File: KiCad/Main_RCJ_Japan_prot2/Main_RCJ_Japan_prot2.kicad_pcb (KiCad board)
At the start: 2 copper layers, 13 parts, among them J1 Conn_01x04_Socket, J2 Conn_01x04_Socket, J3 Conn_01x04_Socket, J4 Conn_01x04_Socket, J5 Conn_01x04_Socket, J6 Conn_01x04_Socket

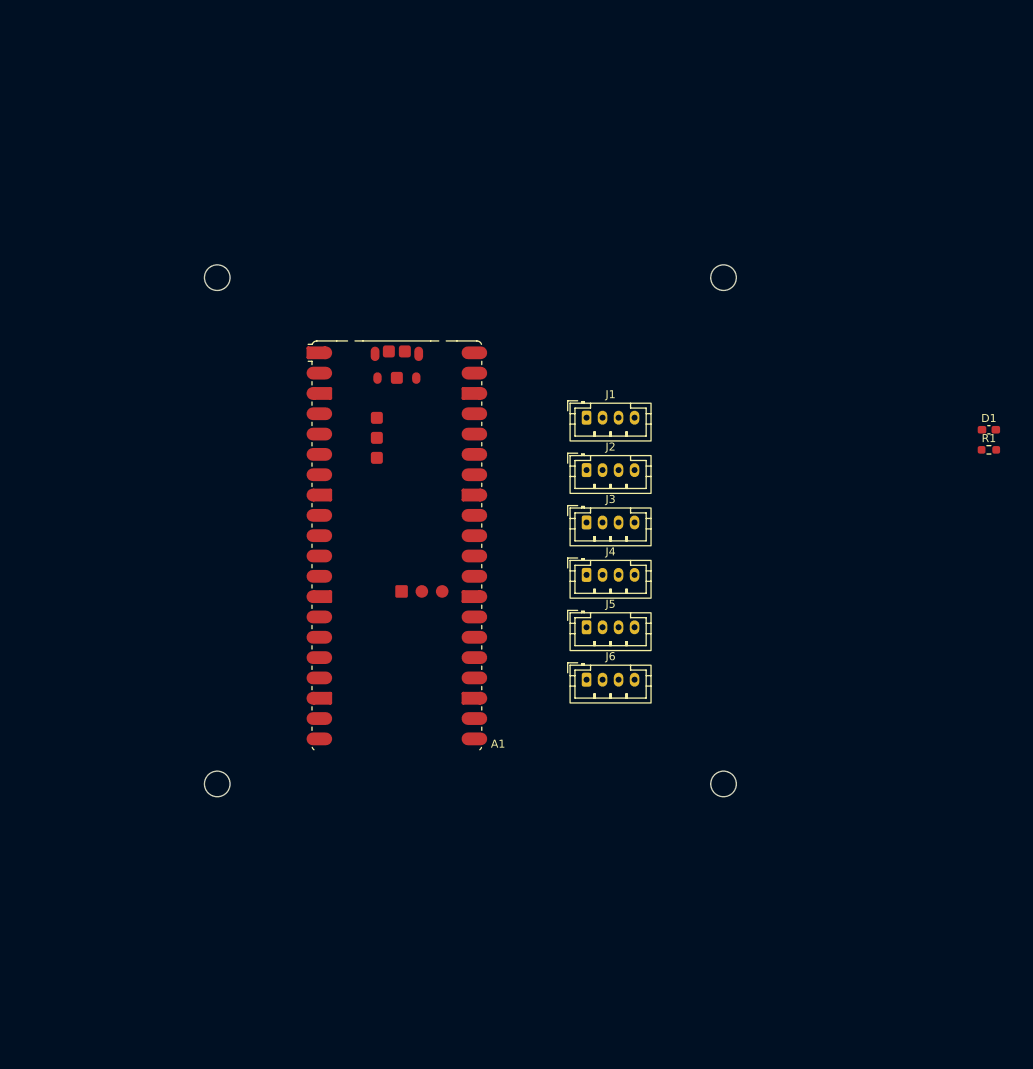
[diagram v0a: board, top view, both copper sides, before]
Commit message: 新メイン仮配置完了
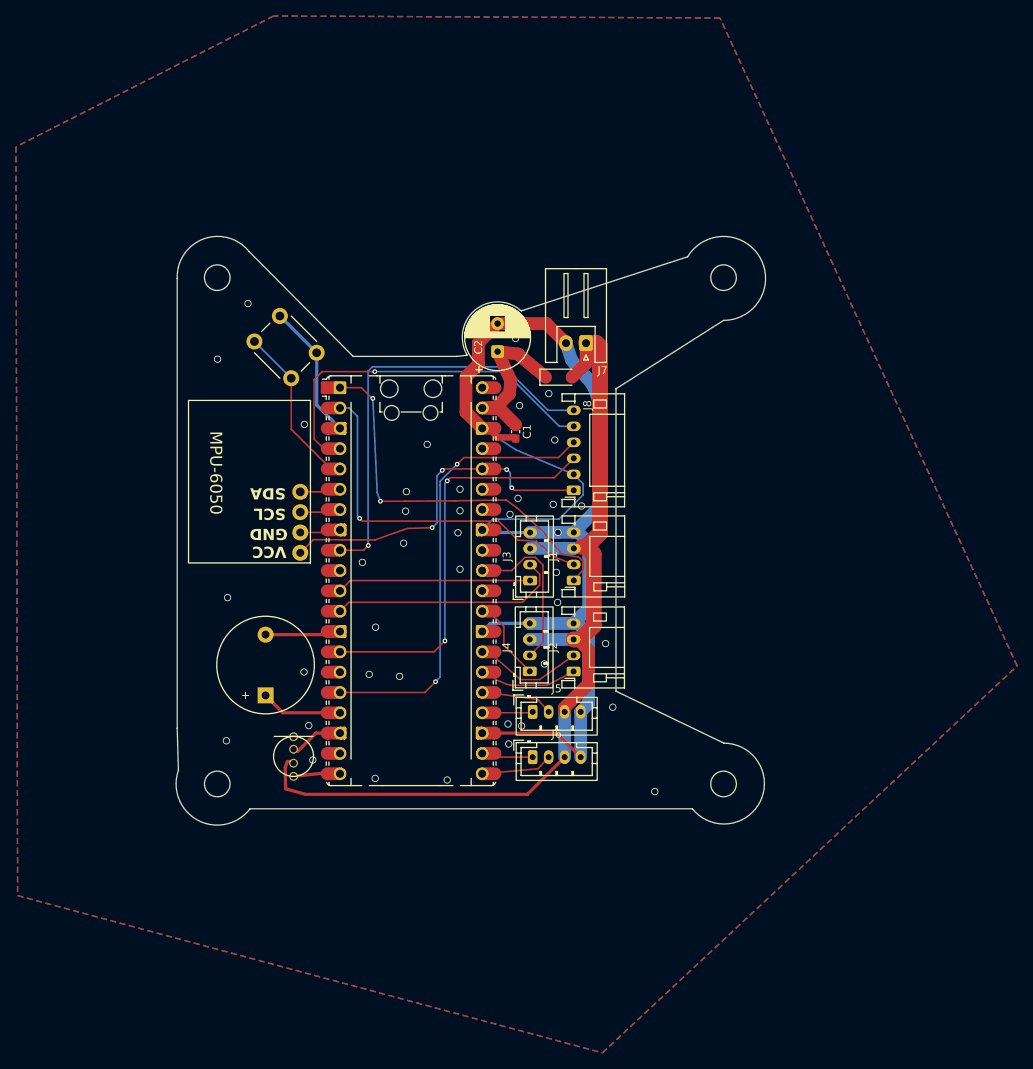
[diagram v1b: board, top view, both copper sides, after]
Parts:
- removed D1: LED, Capacitor_SMD:C_0603_1608Metric_Pad1.08x0.95mm_HandSolder
- removed R1: R, Resistor_SMD:R_0603_1608Metric_Pad0.98x0.95mm_HandSolder
- added BZ1: Buzzer, Buzzer_Beeper:Buzzer_12x9.5RM7.6, F.Cu at (74.4, 120.6)
- added C1: C, Capacitor_SMD:C_0603_1608Metric_Pad1.08x0.95mm_HandSolder, F.Cu at (105.7, 87.6)
- added C2: C_Polarized_US, Capacitor_THT:CP_Radial_D8.0mm_P3.50mm, F.Cu at (103.4, 77.6)
- added D2: D_Schottky, Diode_SMD:D_SOD-123, F.Cu at (111.0, 80.8)
- added J7: Conn_01x02_Socket, Connector_JST:JST_XH_S2B-XH-A_1x02_P2.50mm_Horizontal, F.Cu at (114.5, 76.5)
- added J8: Conn_01x06_Socket, Connector_JST:JST_PH_S6B-PH-K_1x06_P2.00mm_Horizontal, F.Cu at (112.9, 94.9)
- added SW1: SW_Push, Button_Switch_THT:SW_PUSH_6mm, F.Cu at (76.2, 73.2)
- added U1: ~, MPU:名称未設定, F.Cu at (73.7, 97.7)
- added U2: ~, PL9823-F5(RGBLED):名称未設定, F.Cu at (77.9, 128.2)
- A1: footprint Module:RaspberryPi_Pico_W_SMD -> Module:RaspberryPi_Pico_Common_Unspecified
- J1, J2: footprint Connector_JST:JST_PH_B4B-PH-K_1x04_P2.00mm_Vertical -> Connector_JST:JST_PH_S4B-PH-K_1x04_P2.00mm_Horizontal
- moved J2 25.2 mm to (112.9, 117.6), turned to 90 degrees
- moved J1 20.4 mm to (112.9, 106.2), turned to 90 degrees
- moved J4 14.0 mm to (107.4, 117.6), turned to 90 degrees
- moved J5 12.5 mm to (107.8, 122.6)
- moved J6 11.8 mm to (107.8, 128.3)
- moved J3 10.1 mm to (107.5, 106.2), turned to 90 degrees
- moved A1 4.71 mm to (92.6, 106.2)
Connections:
- A1 pad 14: unconnected-(A1-GPIO10-Pad14) -> kicker_in1
- A1 pad 16: unconnected-(A1-GPIO12-Pad16) -> kicker_in2
- A1 pad 17: unconnected-(A1-GPIO13-Pad17) -> Net-(A1-GPIO13)
- A1 pad 20: unconnected-(A1-GPIO15-Pad20) -> Net-(A1-GPIO15)
- A1 pad 21: unconnected-(A1-GPIO16-Pad21) -> PIO-UART3_RX
- A1 pad 22: unconnected-(A1-GPIO17-Pad22) -> PIO-UART3_TX
- A1 pad 24: unconnected-(A1-GPIO18-Pad24) -> PIO-UART2_TX
- A1 pad 25: unconnected-(A1-GPIO19-Pad25) -> PIO-UART2_RX
- A1 pad 26: unconnected-(A1-GPIO20-Pad26) -> PIO-UART0_TX
- A1 pad 27: unconnected-(A1-GPIO21-Pad27) -> PIO-UART0_RX
- A1 pad 29: unconnected-(A1-GPIO22-Pad29) -> PIO-UART1_TX
- A1 pad 31: unconnected-(A1-GPIO26_ADC0-Pad31) -> PIO-UART1_RX
- A1 pad 36: unconnected-(A1-3V3-Pad36) -> 3v3
- A1 pad 39: VCC -> Net-(A1-VSYS)
- A1 pad 4: unconnected-(A1-GPIO2-Pad4) -> kicker_in3
- A1 pad 5: unconnected-(A1-GPIO3-Pad5) -> Net-(A1-GPIO3)
- A1 pad 9: unconnected-(A1-GPIO6-Pad9) -> kicker_in4
- J1 pad 1: unconnected-(J1-Pin_1-Pad1) -> UART0_TX
- J1 pad 2: unconnected-(J1-Pin_2-Pad2) -> UART0_RX
- J1 pad 3: unconnected-(J1-Pin_3-Pad3) -> VCC
- J1 pad 4: unconnected-(J1-Pin_4-Pad4) -> GND
- J2 pad 1: unconnected-(J2-Pin_1-Pad1) -> PIO-UART0_TX
- J2 pad 2: unconnected-(J2-Pin_2-Pad2) -> PIO-UART0_RX
- J2 pad 3: unconnected-(J2-Pin_3-Pad3) -> VCC
- J2 pad 4: unconnected-(J2-Pin_4-Pad4) -> GND
- J3 pad 1: unconnected-(J3-Pin_1-Pad1) -> H-UART1_TX
- J3 pad 2: unconnected-(J3-Pin_2-Pad2) -> H-UART1_RX
- J3 pad 3: unconnected-(J3-Pin_3-Pad3) -> VCC
- J3 pad 4: unconnected-(J3-Pin_4-Pad4) -> GND
- J4 pad 1: unconnected-(J4-Pin_1-Pad1) -> PIO-UART1_TX
- J4 pad 2: unconnected-(J4-Pin_2-Pad2) -> PIO-UART1_RX
- J4 pad 3: unconnected-(J4-Pin_3-Pad3) -> VCC
- J4 pad 4: unconnected-(J4-Pin_4-Pad4) -> GND
- J5 pad 1: unconnected-(J5-Pin_1-Pad1) -> PIO-UART2_TX
- J5 pad 2: unconnected-(J5-Pin_2-Pad2) -> PIO-UART2_RX
- J5 pad 3: unconnected-(J5-Pin_3-Pad3) -> VCC
- J5 pad 4: unconnected-(J5-Pin_4-Pad4) -> GND
- J6 pad 1: unconnected-(J6-Pin_1-Pad1) -> PIO-UART3_TX
- J6 pad 2: unconnected-(J6-Pin_2-Pad2) -> PIO-UART3_RX
- J6 pad 3: unconnected-(J6-Pin_3-Pad3) -> VCC
- J6 pad 4: unconnected-(J6-Pin_4-Pad4) -> GND
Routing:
- net GND: track 0.00 -> 193.3 mm, vias 0 -> 40
- net VCC: track 0.00 -> 115.8 mm
- net kicker_in2: track 0.00 -> 57.1 mm, vias 0 -> 2
- net kicker_in4: track 0.00 -> 53.8 mm, vias 0 -> 1
- net kicker_in1: track 0.00 -> 50.8 mm, vias 0 -> 2
- net UART0_TX: track 0.00 -> 48.8 mm, vias 0 -> 2
- net kicker_in3: track 0.00 -> 46.1 mm, vias 0 -> 1
- net UART0_RX: track 0.00 -> 44.7 mm, vias 0 -> 1
- net 3v3: track 0.00 -> 43.7 mm, vias 0 -> 4
- net H-UART1_RX: track 0.00 -> 29.4 mm
- net H-UART1_TX: track 0.00 -> 24.3 mm
- net Net-(A1-VSYS): track 0.00 -> 21.1 mm
- net Net-(A1-GPIO3): track 0.00 -> 21.0 mm
- net PIO-UART1_RX: track 0.00 -> 20.6 mm
- net PIO-UART0_RX: track 0.00 -> 12.9 mm
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- added copper zone on B.Cu, net GND
- added copper zone on F.Cu, net GND
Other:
- board outline added: 73.7 x 73.6 mm

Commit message: 新メイン完成
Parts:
- added C3: C, Capacitor_SMD:C_0603_1608Metric_Pad1.08x0.95mm_HandSolder, F.Cu at (66.1, 109.6)
- added G***: LOGO, LOGO:名称未設定, F.Cu at (86.5, 137.8)
- added G***: LOGO, LOGO:ICON, F.Cu at (96.6, 144.1)
- added G***: LOGO, LOGO:logo, F.Cu at (111.7, 59.4)
- added J10: Conn_01x02_Socket, Connector_JST:JST_XH_S2B-XH-A_1x02_P2.50mm_Horizontal, F.Cu at (124.6, 137.7)
- added J11: Conn_01x03_Socket, Connector_JST:JST_PH_B3B-PH-K_1x03_P2.00mm_Vertical, F.Cu at (99.9, 127.2)
- added J12: Conn_01x03_Socket, Connector_JST:JST_PH_B3B-PH-K_1x03_P2.00mm_Vertical, F.Cu at (99.9, 115.6)
- added J13: Conn_01x02_Socket, Connector_JST:JST_PH_B2B-PH-K_1x02_P2.00mm_Vertical, F.Cu at (100.9, 121.4)
- added J14: Conn_01x02_Socket, Connector_JST:JST_PH_B2B-PH-K_1x02_P2.00mm_Vertical, F.Cu at (100.3, 133.2)
- added J9: Conn_02x03_Odd_Even, Connector_PinHeader_2.54mm:PinHeader_2x03_P2.54mm_Vertical, F.Cu at (60.3, 77.5)
- added R1: R, Resistor_THT:R_Axial_DIN0309_L9.0mm_D3.2mm_P12.70mm_Horizontal, F.Cu at (116.9, 139.2)
- added R2: R, Resistor_THT:R_Axial_DIN0309_L9.0mm_D3.2mm_P12.70mm_Horizontal, F.Cu at (118.3, 143.5)
- moved SW1 54.0 mm to (80.6, 127.0), turned to 0 degrees
- moved J8 24.1 mm to (98.0, 76.0)
- moved BZ1 18.0 mm to (59.3, 110.7), turned to -90 degrees
- moved C1 16.9 mm to (91.7, 78.1)
- moved J3 15.6 mm to (94.0, 98.4)
- moved A1 15.6 mm to (79.1, 98.5)
- moved J1 15.6 mm to (99.5, 98.4)
- moved J2 15.6 mm to (99.4, 109.8)
- moved J4 15.6 mm to (94.0, 109.8)
- moved J7 15.5 mm to (102.8, 86.8), turned to 90 degrees
- moved J6 14.3 mm to (94.0, 132.0), turned to 90 degrees
- moved J5 13.9 mm to (94.0, 120.9), turned to 90 degrees
- moved U1 13.0 mm to (61.1, 101.0)
- moved D2 11.0 mm to (100.1, 80.0)
- moved C2 10.0 mm to (95.4, 83.7), turned to -90 degrees
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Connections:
- A1 pad 10: unconnected-(A1-GPIO7-Pad10) -> Net-(A1-GPIO7)
- A1 pad 15: unconnected-(A1-GPIO11-Pad15) -> PIO-UART1_RX
- A1 pad 19: unconnected-(A1-GPIO14-Pad19) -> Net-(A1-GPIO14)
- A1 pad 31: PIO-UART1_RX -> ADC1
- A1 pad 32: unconnected-(A1-GPIO27_ADC1-Pad32) -> ADC2
- A1 pad 34: unconnected-(A1-GPIO28_ADC2-Pad34) -> BATT_ADC
- U2 pad 3: VCC -> Net-(A1-VSYS)
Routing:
- net 3v3: track 43.7 -> 148.9 mm, vias 4 -> 3
- net Net-(A1-VSYS): track 21.1 -> 126.0 mm, vias 0 -> 1
- net BATT_ADC: track 0.00 -> 68.5 mm, vias 0 -> 3
- net ADC1: track 0.00 -> 52.8 mm
- net GND: track 193.3 -> 245.9 mm, vias 40 -> 69
- net Net-(A1-GPIO14): track 0.00 -> 49.4 mm
- net ADC2: track 0.00 -> 48.6 mm
- net VCC: track 115.8 -> 72.3 mm
- net Net-(A1-GPIO3): track 21.0 -> 59.4 mm, vias 0 -> 1
- net Net-(A1-GPIO7): track 0.00 -> 17.6 mm
- net Net-(J10-Pin_1): track 0.00 -> 14.1 mm
- net SDA: track 4.30 -> 15.4 mm
- net PIO-UART3_TX: track 6.50 -> 17.5 mm
- net SCL: track 4.30 -> 14.0 mm
- net kicker_in1: track 50.8 -> 59.0 mm, vias 2 -> 1
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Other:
- board size 73.7 x 73.6 mm -> 99.5 x 94.9 mm
- board text added: "+ -"
- board text added: "- +"
- board text added: "1 0 5V GND"
- board text added: "16 17 5V GND"
- board text added: "18 19 5V GND"
- board text added: "20 21 5V GND"
- board text added: "22 11 5V GND"
- board text added: "26 GND 3v3"
- board text added: "27 GND 3V3"
- board text added: "3v3 GND 7"
- board text added: "5V GND 14"
- board text added: "6 2 12 10 GND 3v3"
- board text added: "8 9 5V GND"
- board text added: "GND 3v3"
- board text added: "GND 5V"
- board text added: "GND VCC+"
- board text added: "SDA ⇒ GP4 SCL ⇒ GP5"
- board text added: "Sound ⇒ 13 LED ⇒ 15 SW ⇒ 3"
